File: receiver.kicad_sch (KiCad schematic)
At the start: 0 parts

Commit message: Polished IO schematics
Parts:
- added U38: STM32H723ZGTx, Package_QFP:LQFP-144_20x20mm_P0.5mm, symbol MCU_ST_STM32H7:STM32H723ZGTx
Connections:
- new net: U38.107 (VSS), U38.120 (VSS), U38.130 (VSS), U38.16 (VSS), U38.38 (VSS), U38.51 (VSS), U38.61 (VSS), U38.83 (VSS), U38.94 (VSS)
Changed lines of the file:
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@@
 (kicad_sch (version 20230121) (generator eeschema)
-  (paper "A4")
-)
+  (paper "A4" portrait)

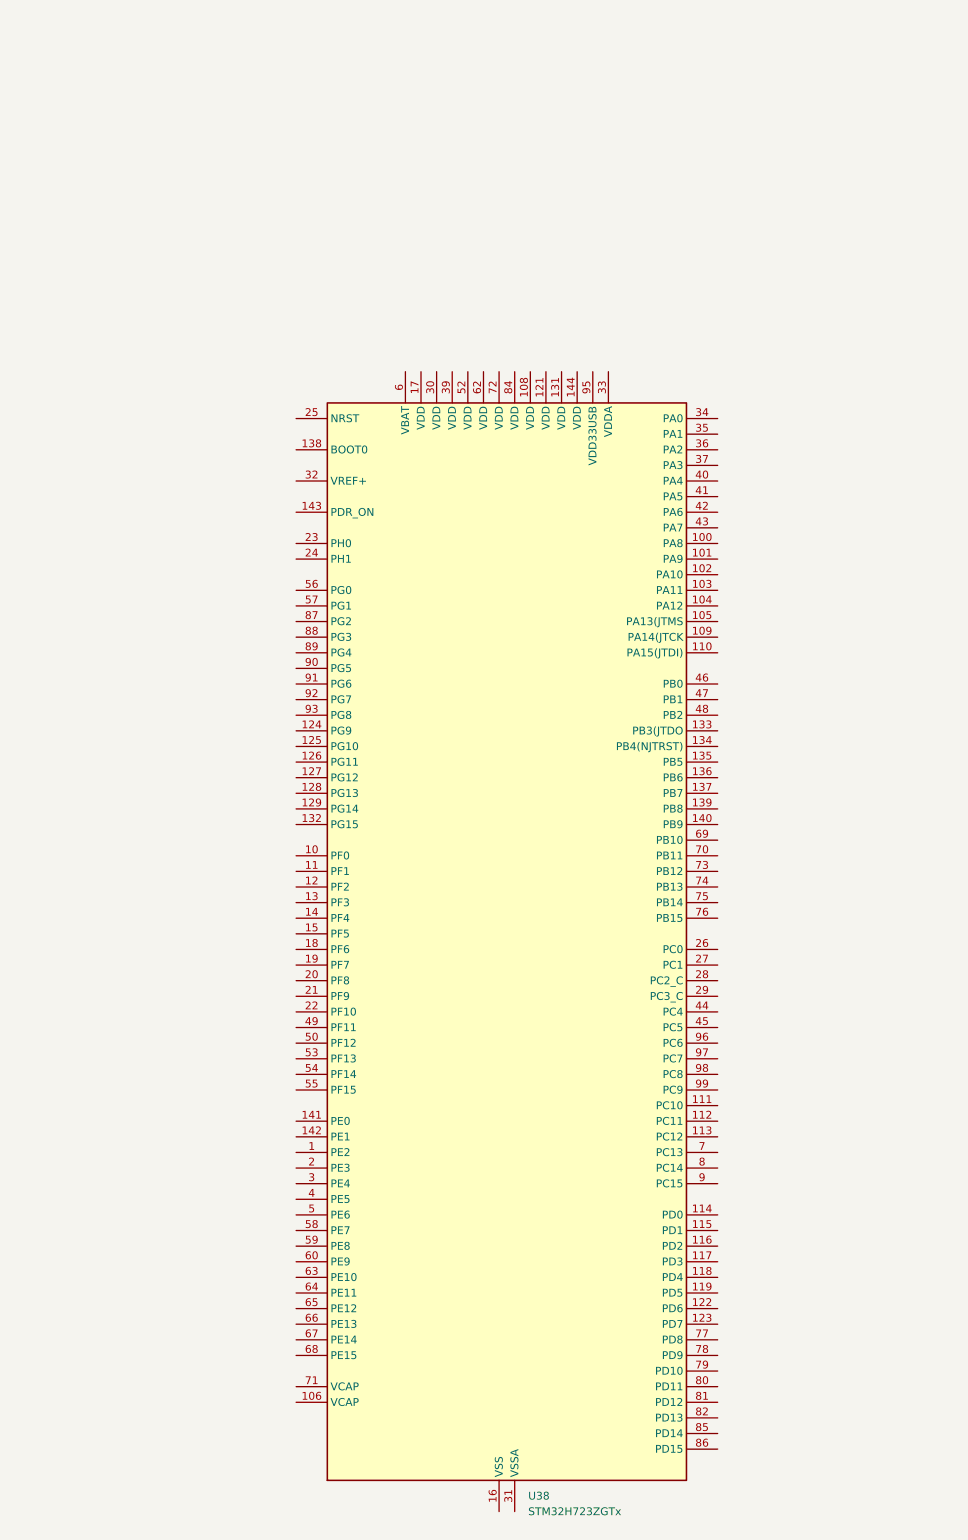
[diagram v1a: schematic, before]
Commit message: Set power routing for stm32
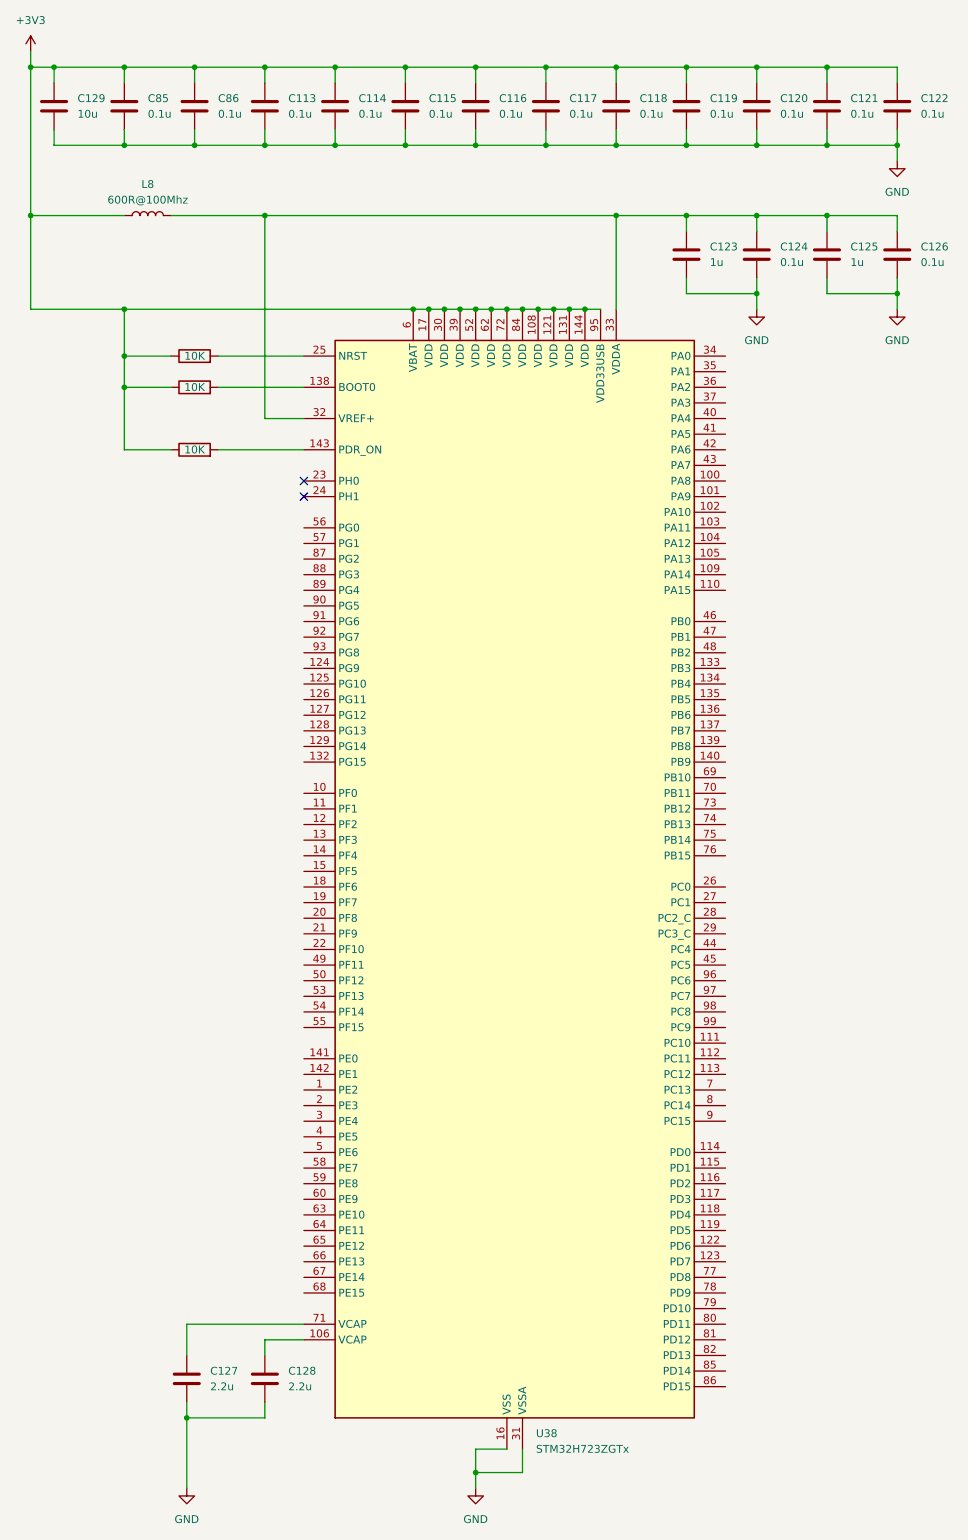
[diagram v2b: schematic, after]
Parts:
- added C113, C114, C115, C116, C117, C118, C119, C120, C121, C122, C124, C126, C85, C86: 0.1u, symbol Device:C
- added C123, C125: 1u, symbol Device:C
- added C127, C128: 2.2u, symbol Device:C
- added C129: 10u, symbol Device:C
- added L8: 600R@100Mhz, symbol Device:L
- added R190, R193, R194: 10K, symbol Device:R
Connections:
- net at U38.106 (VCAP): now also C128.1
- net GND: now reaches U38.107 (VSS), U38.120 (VSS), U38.130 (VSS), U38.16 (VSS), U38.38 (VSS), U38.51 (VSS), U38.61 (VSS), U38.83 (VSS), U38.94 (VSS)
- net GND: now also U38.31 (VSSA), C113.2, C114.2, C115.2, C116.2, C117.2, C118.2, C119.2, C120.2, C121.2, C122.2, C123.2, C124.2, C125.2, C126.2, C127.2, C128.2, C129.2, C85.2, C86.2
- net +3V3: now reaches U38.108 (VDD)
- net +3V3: now also U38.121 (VDD), U38.131 (VDD), U38.144 (VDD), U38.17 (VDD), U38.30 (VDD), U38.39 (VDD), U38.52 (VDD), U38.6 (VBAT), U38.62 (VDD), U38.72 (VDD), U38.84 (VDD), U38.95 (VDD33USB), C113.1, C114.1, C115.1, C116.1, C117.1, C118.1, C119.1, C120.1, C121.1, C122.1, C129.1, C85.1, C86.1, L8.1, R190.1, R193.1, R194.1
- net at U38.138 (BOOT0): now also R193.2
- net at U38.143 (PDR_ON): now also R194.2
- net at U38.25 (NRST): now also R190.2
- net at U38.32 (VREF+): now also U38.33 (VDDA), C123.1, C124.1, C125.1, C126.1, L8.2
- net at U38.71 (VCAP): now also C127.1
- no-connect marks 0 -> 2

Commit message: Assigned proper footprints for all components
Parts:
- removed C125: 1u, symbol Device:C
- removed C126: 0.1u, symbol Device:C
- C113, C114, C115, C116, C117, C118, C119, C120, C121, C122, C124, C85, C86: value 0.1u -> 100n; footprint (none) -> Capacitor_SMD:C_0603_1608Metric_Pad1.08x0.95mm_HandSolder
- C123, C127, C128: footprint (none) -> Capacitor_SMD:C_0805_2012Metric_Pad1.18x1.45mm_HandSolder
- C129: footprint (none) -> Capacitor_SMD:C_1206_3216Metric_Pad1.33x1.80mm_HandSolder
- L8: footprint (none) -> Inductor_SMD:L_0603_1608Metric_Pad1.05x0.95mm_HandSolder
- R190, R193, R194: footprint (none) -> Resistor_SMD:R_0603_1608Metric_Pad0.98x0.95mm_HandSolder
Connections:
- net at C123.1, C124.1, L8.2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: no longer U38.32 (VREF+)
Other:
- moved on the sheet: L8

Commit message: Updated boards hierarchy
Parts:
- renumbered C123 to C112, C124 to C113, C127 to C114, C128 to C115, C129 to C39, C85 to C41, C86 to C76, C113 to C78, C114 to C80, C115 to C82, C116 to C84, C117 to C85, C118 to C86, C119 to C88, C120 to C90, C121 to C92, C122 to C94, L8 to L4, R190 to R194, R193 to R196, R194 to R198, U38 to U17

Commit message: Finished annotation
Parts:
- renumbered C39 to C701, C41 to C702, C76 to C703, C78 to C704, C80 to C705, C82 to C706, C84 to C707, C85 to C708, C86 to C709, C88 to C710, C90 to C711, C92 to C712, C94 to C713, C112 to C714, C113 to C715, C114 to C716, C115 to C717, L4 to L701, R194 to R701, R196 to R702, R198 to R703, U17 to U701
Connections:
- net DOUT1_6: now reaches U701.10 (PF0)
- net SWD_IO: now reaches U701.105 (PA13)
- net SWD_CLK: now reaches U701.109 (PA14)
- net DOUT1_5: now reaches U701.11 (PF1)
- net DOUT5_5: now reaches U701.110 (PA15)
- net DOUT5_1: now reaches U701.111 (PC10)
- net DOUT5_2: now reaches U701.112 (PC11)
- net DOUT5_3: now reaches U701.114 (PD0)
- net DOUT5_4: now reaches U701.115 (PD1)
- net DOUT1_4: now reaches U701.12 (PF2)
- net DOUT6_1: now reaches U701.125 (PG10)
- net DOUT6_2: now reaches U701.126 (PG11)
- net DOUT6_3: now reaches U701.127 (PG12)
- net DOUT6_4: now reaches U701.128 (PG13)
- net DOUT1_3: now reaches U701.13 (PF3)
- net DOUT5_6: now reaches U701.133 (PB3)
- net DOUT6_5: now reaches U701.134 (PB4)
- net DOUT6_6: now reaches U701.135 (PB5)
- net DOUT1_2: now reaches U701.14 (PF4)
- net DOUT1_1: now reaches U701.15 (PF5)
- net ETH_MDC: now reaches U701.27 (PC1)
- net ETH_REFCLK: now reaches U701.35 (PA1)
- net ETH_MDIO: now reaches U701.36 (PA2)
- net ETH_CRS: now reaches U701.43 (PA7)
- net ETH_RXD0: now reaches U701.44 (PC4)
- net ETH_RXD1: now reaches U701.45 (PC5)
- net DOUT2_1: now reaches U701.59 (PE8)
- net DOUT2_5: now reaches U701.60 (PE9)
- net DOUT2_2: now reaches U701.63 (PE10)
- net DOUT2_6: now reaches U701.64 (PE11)
- net DOUT2_3: now reaches U701.65 (PE12)
- net DOUT2_4: now reaches U701.66 (PE13)
- net ETH_NRST: now reaches U701.69 (PB10)
- net ETH_TXEN: now reaches U701.70 (PB11)
- net ETH_TXD0: now reaches U701.73 (PB12)
- net ETH_TXD1: now reaches U701.74 (PB13)
- net DOUT3_1: now reaches U701.77 (PD8)
- net DOUT3_2: now reaches U701.78 (PD9)
- net DOUT3_3: now reaches U701.79 (PD10)
- net DOUT3_4: now reaches U701.80 (PD11)
- net DOUT3_5: now reaches U701.81 (PD12)
- net DOUT3_6: now reaches U701.82 (PD13)
- net DOUT4_1: now reaches U701.90 (PG5)
- net DOUT4_2: now reaches U701.91 (PG6)
- net DOUT4_3: now reaches U701.92 (PG7)
- net DOUT4_4: now reaches U701.93 (PG8)
- net DOUT4_5: now reaches U701.96 (PC6)
- net DOUT4_6: now reaches U701.97 (PC7)
- no-connect marks 2 -> 67
